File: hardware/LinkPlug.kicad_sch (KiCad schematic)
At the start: 4 parts, among them J301 2x05_Horizontal, U301 THVD24x2

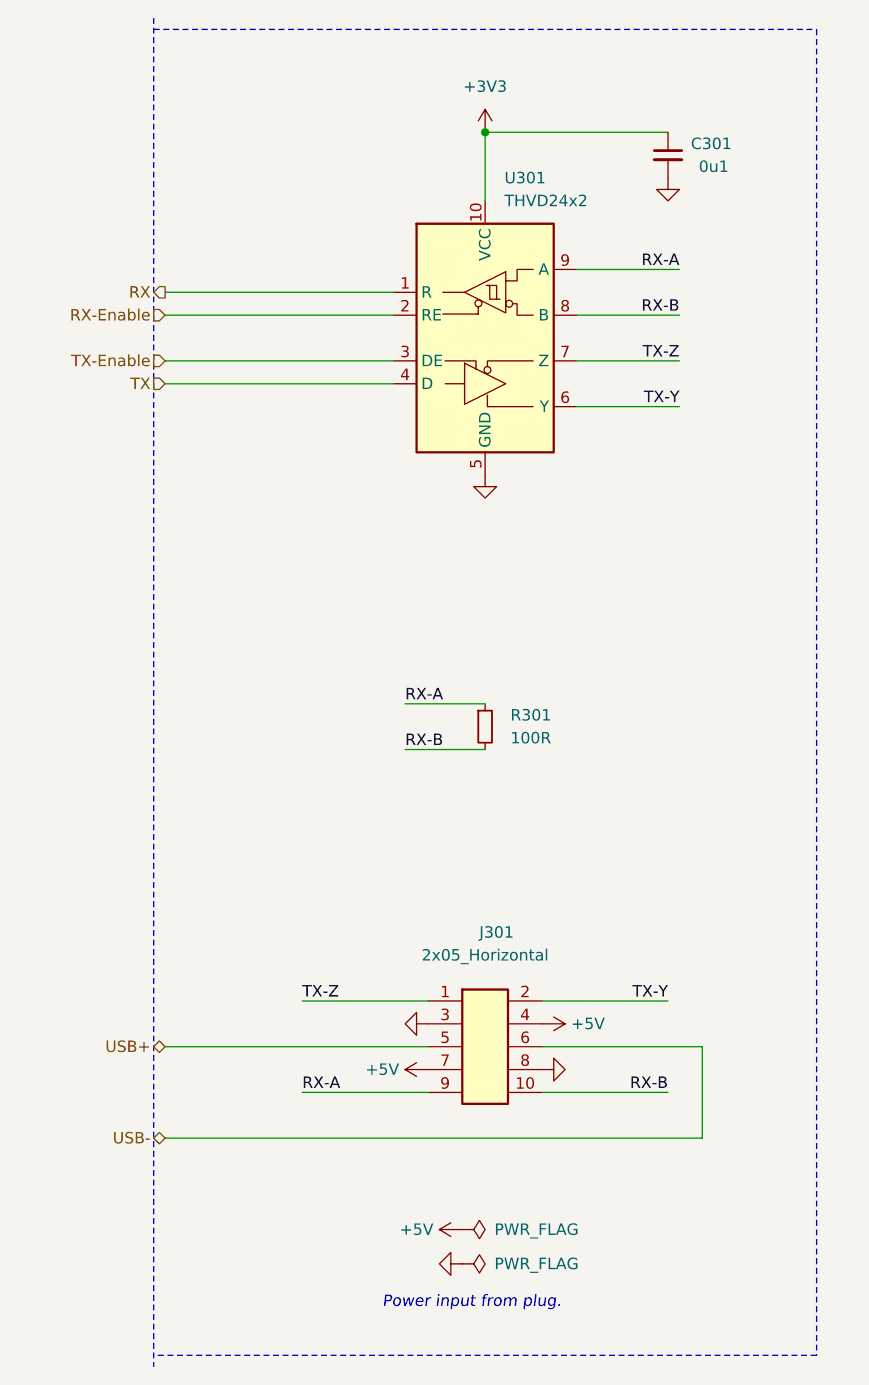
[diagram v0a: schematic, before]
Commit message: Replace Order_Number
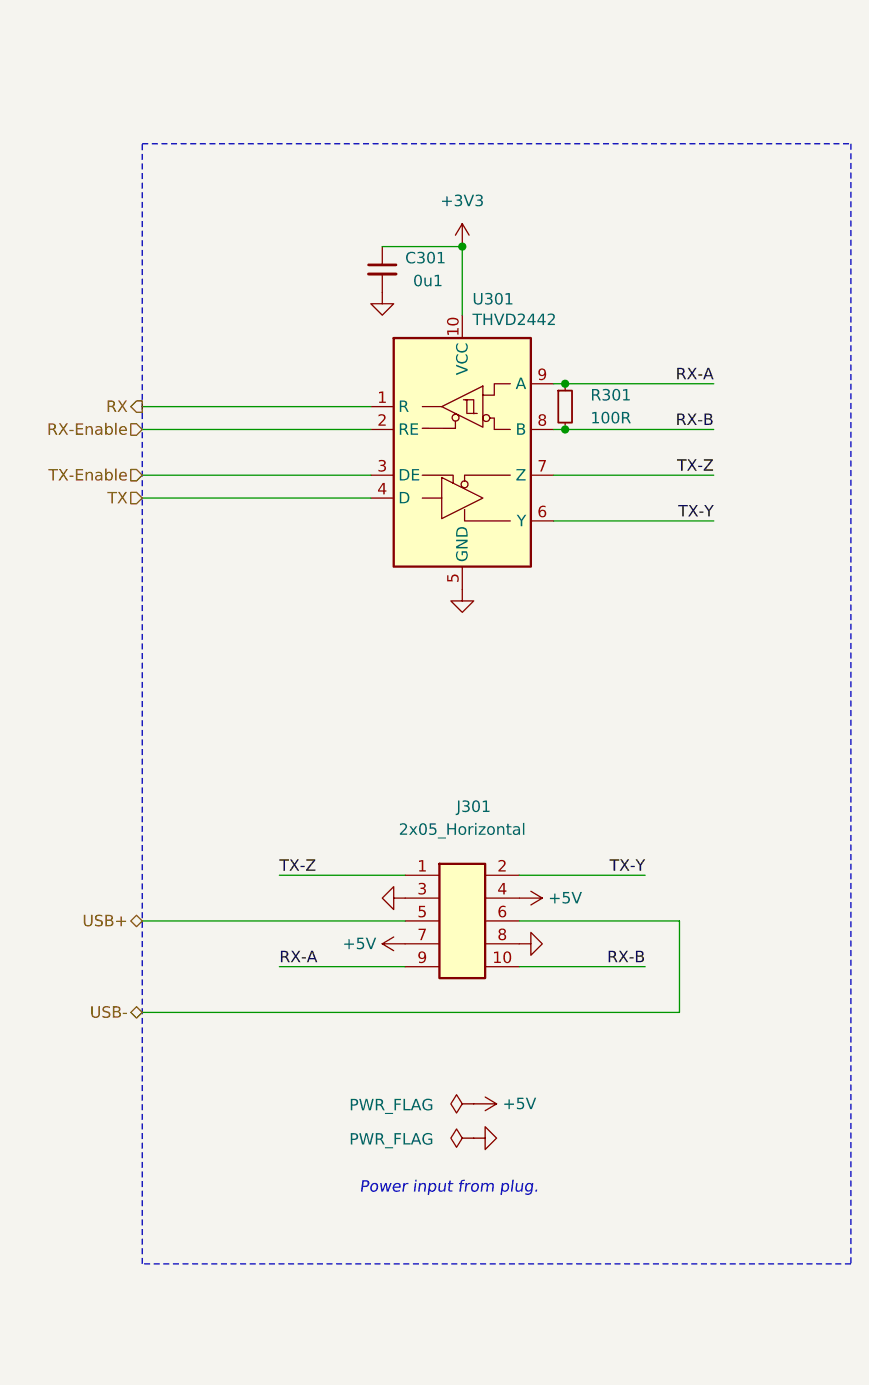
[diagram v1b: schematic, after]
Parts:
- C301: footprint Capacitor_SMD:C_0603_1608Metric -> V2_Capacitor_SMD:C_0603; symbol Device:C_Small -> V2_Device:C_0603_0u1; Manufacturer (none) -> TDK; Mouser (none) -> 810-CGA3E2X7R1H104MA; Product (none) -> CGA3E2X7R1H104M080AA; Rating (none) -> 50V
- J301: Manufacturer (none) -> Amphenol FCI; Mouser (none) -> 649-200211120001T4LF; Product (none) -> 20021112-00010T4LF
- R301: footprint Resistor_SMD:R_0603_1608Metric -> V2_Resistor_SMD:R_0603; symbol Device:R_Small -> V2_Device:R_0603_100R; Manufacturer (none) -> Vishay; Mouser (none) -> 71-CRCW0603100RFKEAH; Product (none) -> CRCW0603100RFKEAHP; Rating (none) -> 330mW
- U301: value THVD24x2 -> THVD2442; symbol V2_Interface_RS485:THVD24x2 -> V2_Interface_RS485:THVD2442; Manufacturer (none) -> Texas Instruments; Mouser (none) -> 595-THVD2442DRCR; Product (none) -> THVD2442DRCR
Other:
- moved on the sheet: C301, J301, R301, U301

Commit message: Update Library
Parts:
- C301: symbol V2_Device:C_0603_0u1 -> V2_Capacitor:0603_0u1
- R301: symbol V2_Device:R_0603_100R -> V2_Resistor:0603_100R
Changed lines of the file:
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@@
 		(on_board yes)
 		(dnp no)
-		(property "Reference" "#PWR0309"
+		(property "Reference" "#PWR309"
 			(at 137.16 66.04 0)
 			(effects
@@
 			(project "wave"
 				(path "/6c8448b4-b04d-47e1-934e-e40cbe27a7be/c6db2f80-f80f-4104-8ca1-02f0ab85cfea"
-					(reference "#PWR0309")
+					(reference "#PWR309")
 					(unit 1)
 				)
@@
 		(on_board yes)
 		(dnp no)
-		(property "Reference" "#FLG0302"
+		(property "Reference" "#FLG302"
 			(at 147.32 151.765 0)
 			(effects
@@
 			(project "wave"
 				(path "/6c8448b4-b04d-47e1-934e-e40cbe27a7be/c6db2f80-f80f-4104-8ca1-02f0ab85cfea"
-					(reference "#FLG0302")
+					(reference "#FLG302")
 					(unit 1)
 				)
@@
 		(on_board yes)
 		(dnp no)
-		(property "Reference" "#FLG0301"
+		(property "Reference" "#FLG301"
 			(at 147.32 147.955 0)
 			(effects
@@
 			(project "wave"
 				(path "/6c8448b4-b04d-47e1-934e-e40cbe27a7be/c6db2f80-f80f-4104-8ca1-02f0ab85cfea"
-					(reference "#FLG0301")
+					(reference "#FLG301")
 					(unit 1)
 				)
@@
 	)
 	(symbol
-		(lib_id "V2_Device:R_0603_100R")
+		(lib_id "V2_Resistor:0603_100R")
 		(at 157.48 72.39 0)
 		(unit 1)
@@
 		(on_board yes)
 		(dnp no)
-		(property "Reference" "#PWR0305"
+		(property "Reference" "#PWR305"
 			(at 143.51 149.86 0)
 			(effects
@@
 			(project "wave"
 				(path "/6c8448b4-b04d-47e1-934e-e40cbe27a7be/c6db2f80-f80f-4104-8ca1-02f0ab85cfea"
-					(reference "#PWR0305")
+					(reference "#PWR305")
 					(unit 1)
 				)
@@
 		(on_board yes)
 		(dnp no)
-		(property "Reference" "#PWR0301"
+		(property "Reference" "#PWR301"
 			(at 133.35 127 0)
 			(effects
@@
 			(project "wave"
 				(path "/6c8448b4-b04d-47e1-934e-e40cbe27a7be/c6db2f80-f80f-4104-8ca1-02f0ab85cfea"
-					(reference "#PWR0301")
+					(reference "#PWR301")
 					(unit 1)
 				)
@@
 		(on_board yes)
 		(dnp no)
-		(property "Reference" "#PWR0302"
+		(property "Reference" "#PWR302"
 			(at 143.51 132.08 0)
 			(effects
@@
 			(project "wave"
 				(path "/6c8448b4-b04d-47e1-934e-e40cbe27a7be/c6db2f80-f80f-4104-8ca1-02f0ab85cfea"
-					(reference "#PWR0302")
+					(reference "#PWR302")
 					(unit 1)
 				)
@@
 		(on_board yes)
 		(dnp no)
-		(property "Reference" "#PWR0304"
+		(property "Reference" "#PWR304"
 			(at 146.05 99.06 0)
 			(effects
@@
 			(project "wave"
 				(path "/6c8448b4-b04d-47e1-934e-e40cbe27a7be/c6db2f80-f80f-4104-8ca1-02f0ab85cfea"
-					(reference "#PWR0304")
+					(reference "#PWR304")
 					(unit 1)
 				)
@@
 		(on_board yes)
 		(dnp no)
-		(property "Reference" "#PWR0307"
+		(property "Reference" "#PWR307"
 			(at 148.59 127 0)
 			(effects
@@
 			(project "wave"
 				(path "/6c8448b4-b04d-47e1-934e-e40cbe27a7be/c6db2f80-f80f-4104-8ca1-02f0ab85cfea"
-					(reference "#PWR0307")
+					(reference "#PWR307")
 					(unit 1)
 				)
@@
 		(on_board yes)
 		(dnp no)
-		(property "Reference" "#PWR0303"
+		(property "Reference" "#PWR303"
 			(at 146.05 58.42 0)
 			(effects
@@
 			(project "wave"
 				(path "/6c8448b4-b04d-47e1-934e-e40cbe27a7be/c6db2f80-f80f-4104-8ca1-02f0ab85cfea"
-					(reference "#PWR0303")
+					(reference "#PWR303")
 					(unit 1)
 				)
@@
 		(on_board yes)
 		(dnp no)
-		(property "Reference" "#PWR0306"
+		(property "Reference" "#PWR306"
 			(at 153.67 153.67 0)
 			(effects
@@
 			(project "wave"
 				(path "/6c8448b4-b04d-47e1-934e-e40cbe27a7be/c6db2f80-f80f-4104-8ca1-02f0ab85cfea"
-					(reference "#PWR0306")
+					(reference "#PWR306")
 					(unit 1)
 				)
@@
 		(on_board yes)
 		(dnp no)
-		(property "Reference" "#PWR0308"
+		(property "Reference" "#PWR308"
 			(at 158.75 132.08 0)
 			(effects
@@
 			(project "wave"
 				(path "/6c8448b4-b04d-47e1-934e-e40cbe27a7be/c6db2f80-f80f-4104-8ca1-02f0ab85cfea"
-					(reference "#PWR0308")
-					(unit 1)
-				)
-			)
-		)
-	)
-	(symbol
-		(lib_id "V2_Device:C_0603_0u1")
+					(reference "#PWR308")
+					(unit 1)
+				)
+			)
+		)
+	)
+	(symbol
+		(lib_id "V2_Capacitor:0603_0u1")
 		(at 137.16 57.15 0)
 		(unit 1)
